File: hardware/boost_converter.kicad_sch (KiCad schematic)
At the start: 10 parts, among them U5 TPS61200DRC

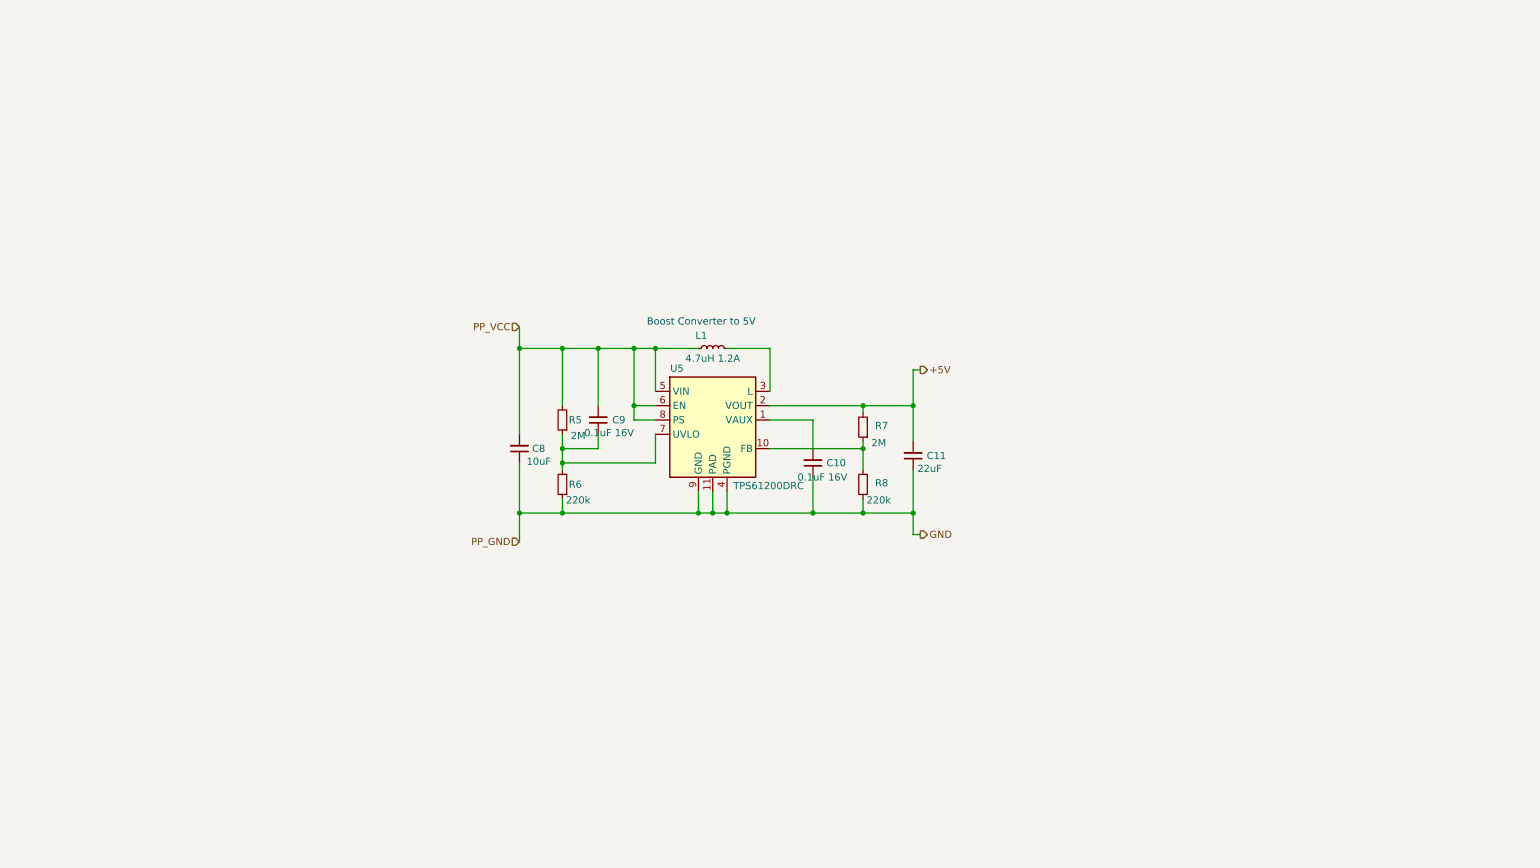
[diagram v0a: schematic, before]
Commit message: Schematic completed, commented and ready for review
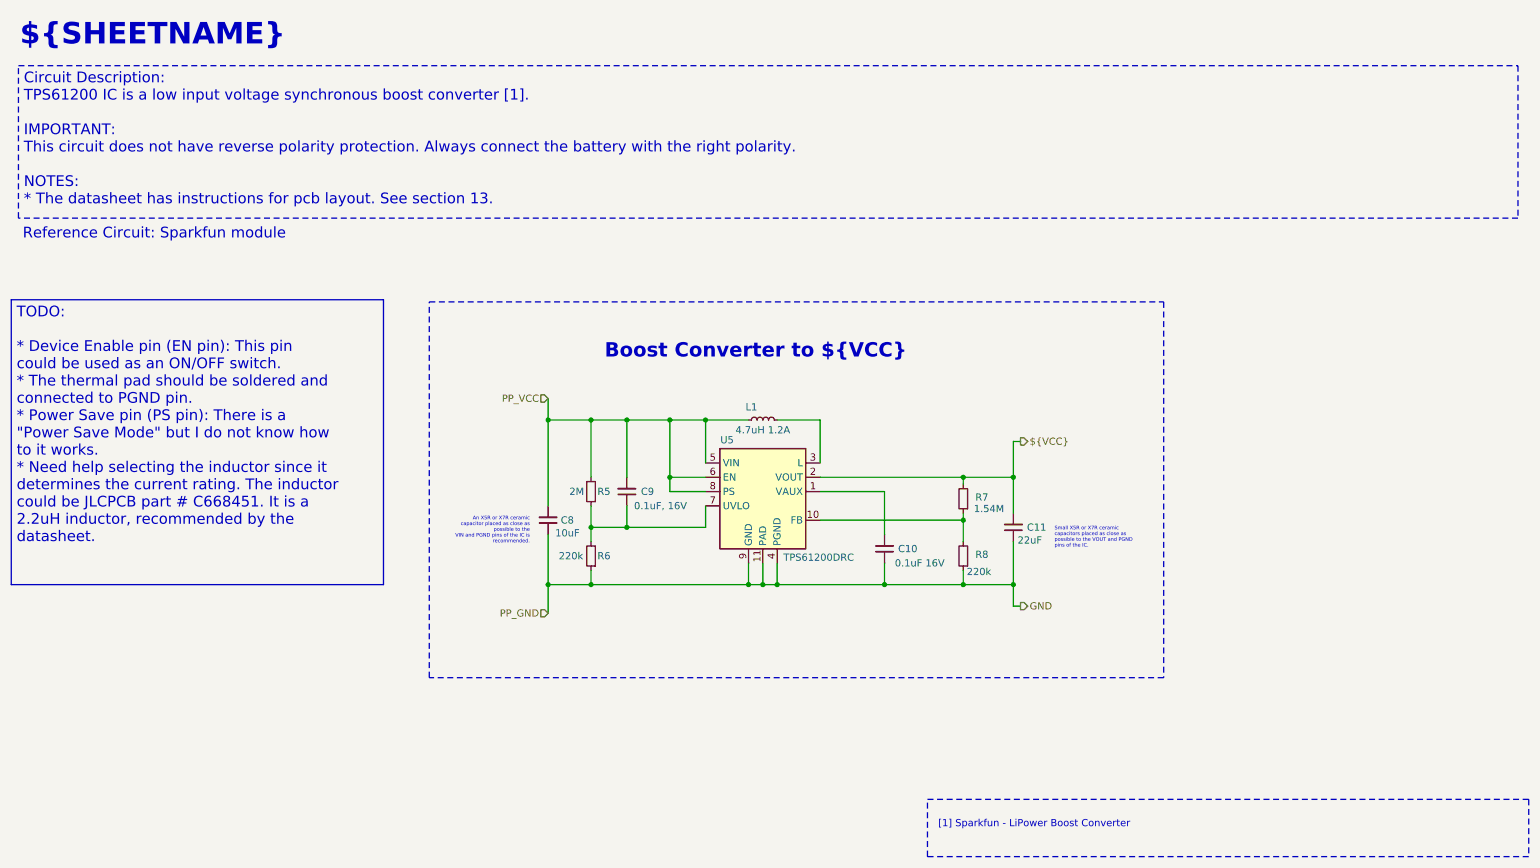
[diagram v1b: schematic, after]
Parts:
- C9: value 0.1uF 16V -> 0.1uF, 16V
- R7: value 2M -> 1.54M
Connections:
- net +5V renamed ${VCC}
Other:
- note added: "${SHEETNAME}"
- note added: "Boost Converter to ${VCC}"
- note added: "Reference Circuit: Sparkfun module"
- note added: "[1] Sparkfun - LiPower Boost Converter"
- note removed: "Boost Converter to 5V"
- title: Kitchen_Timer - 5V Boost Converter -> Kitchen_Timer - ${SHEETNAME}
- moved on the sheet: C10, C11, C8, C9, L1, R5, R6, R7, R8, U5

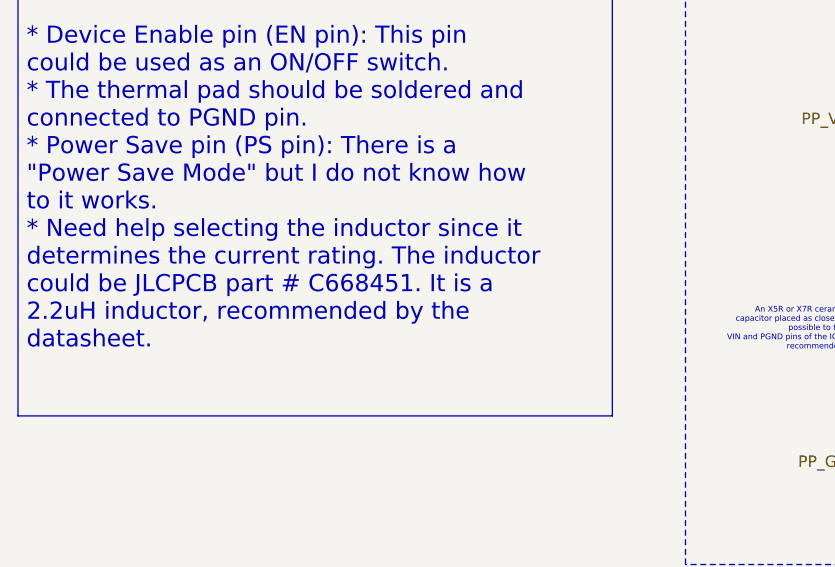
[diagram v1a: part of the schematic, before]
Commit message: Added comments to the TODO boxes after the meeting with Erasmus
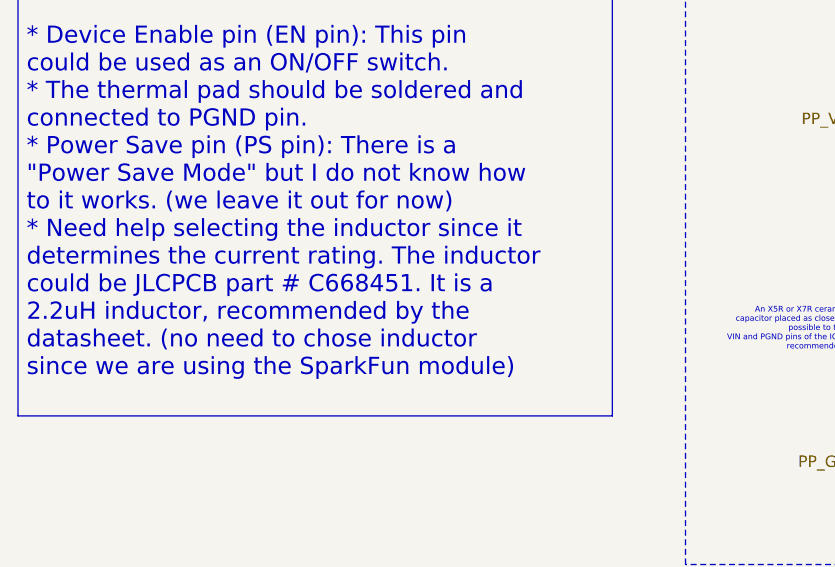
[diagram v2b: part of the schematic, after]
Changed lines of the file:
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@@
 		)
 	)
-	(text_box "TODO:\n\n* Device Enable pin (EN pin): This pin could be used as an ON/OFF switch.\n* The thermal pad should be soldered and connected to PGND pin.\n* Power Save pin (PS pin): There is a \"Power Save Mode\" but I do not know how to it works.\n* Need help selecting the inductor since it determines the current rating. The inductor could be JLCPCB part # C668451. It is a 2.2uH inductor, recommended by the datasheet.\n\n"
+	(text_box "TODO:\n\n* Device Enable pin (EN pin): This pin could be used as an ON/OFF switch.\n* The thermal pad should be soldered and connected to PGND pin.\n* Power Save pin (PS pin): There is a \"Power Save Mode\" but I do not know how to it works. (we leave it out for now)\n* Need help selecting the inductor since it determines the current rating. The inductor could be JLCPCB part # C668451. It is a 2.2uH inductor, recommended by the datasheet. (no need to chose inductor since we are using the SparkFun module)\n\n\n"
 		(exclude_from_sim no)
 		(at 15.24 66.294 0)

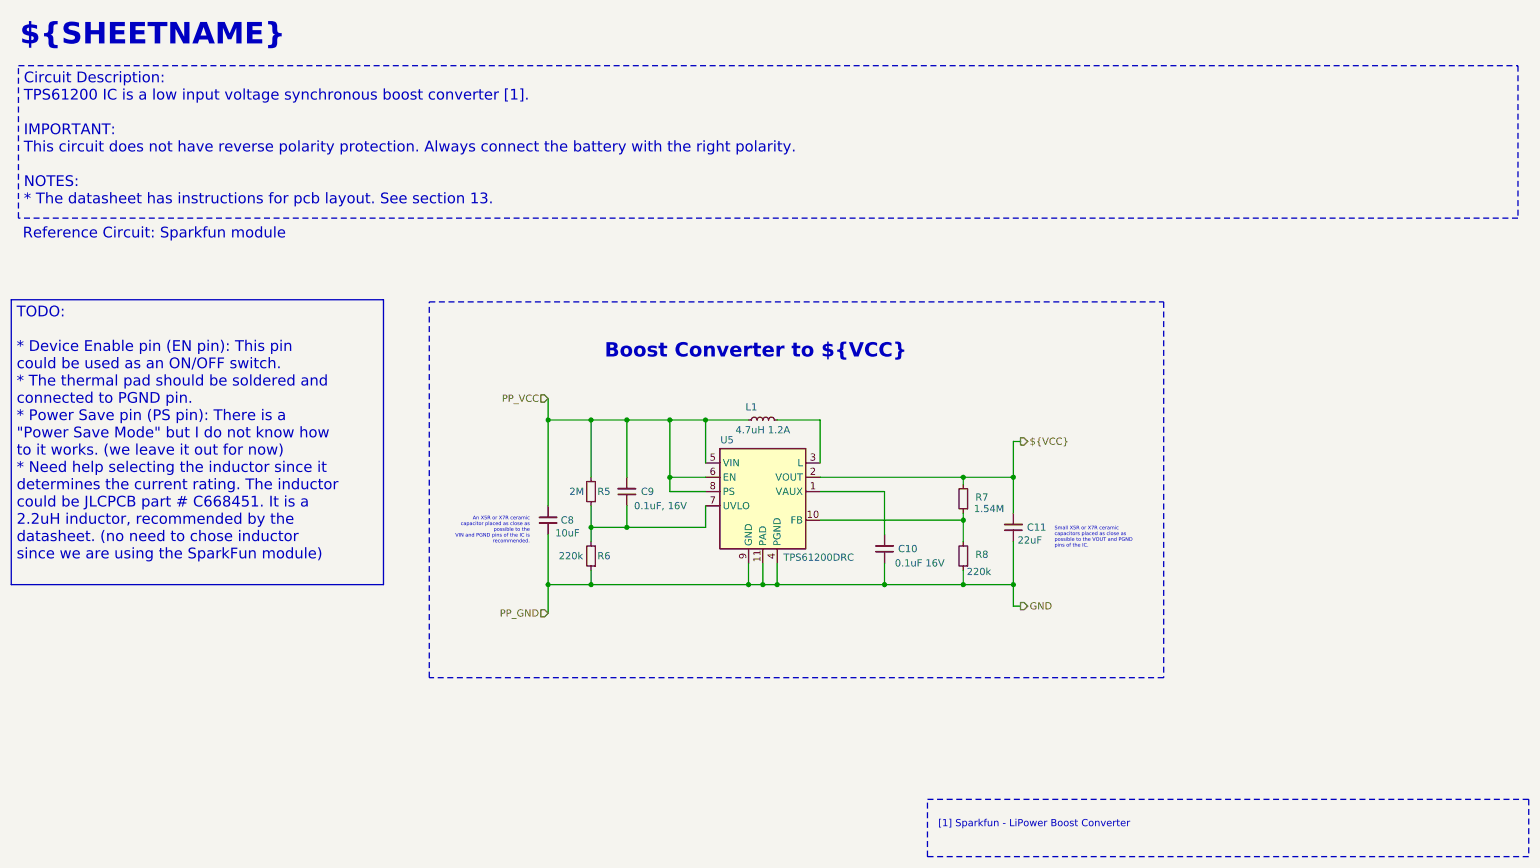
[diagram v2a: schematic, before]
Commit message: Added the Power Switch and Test Points
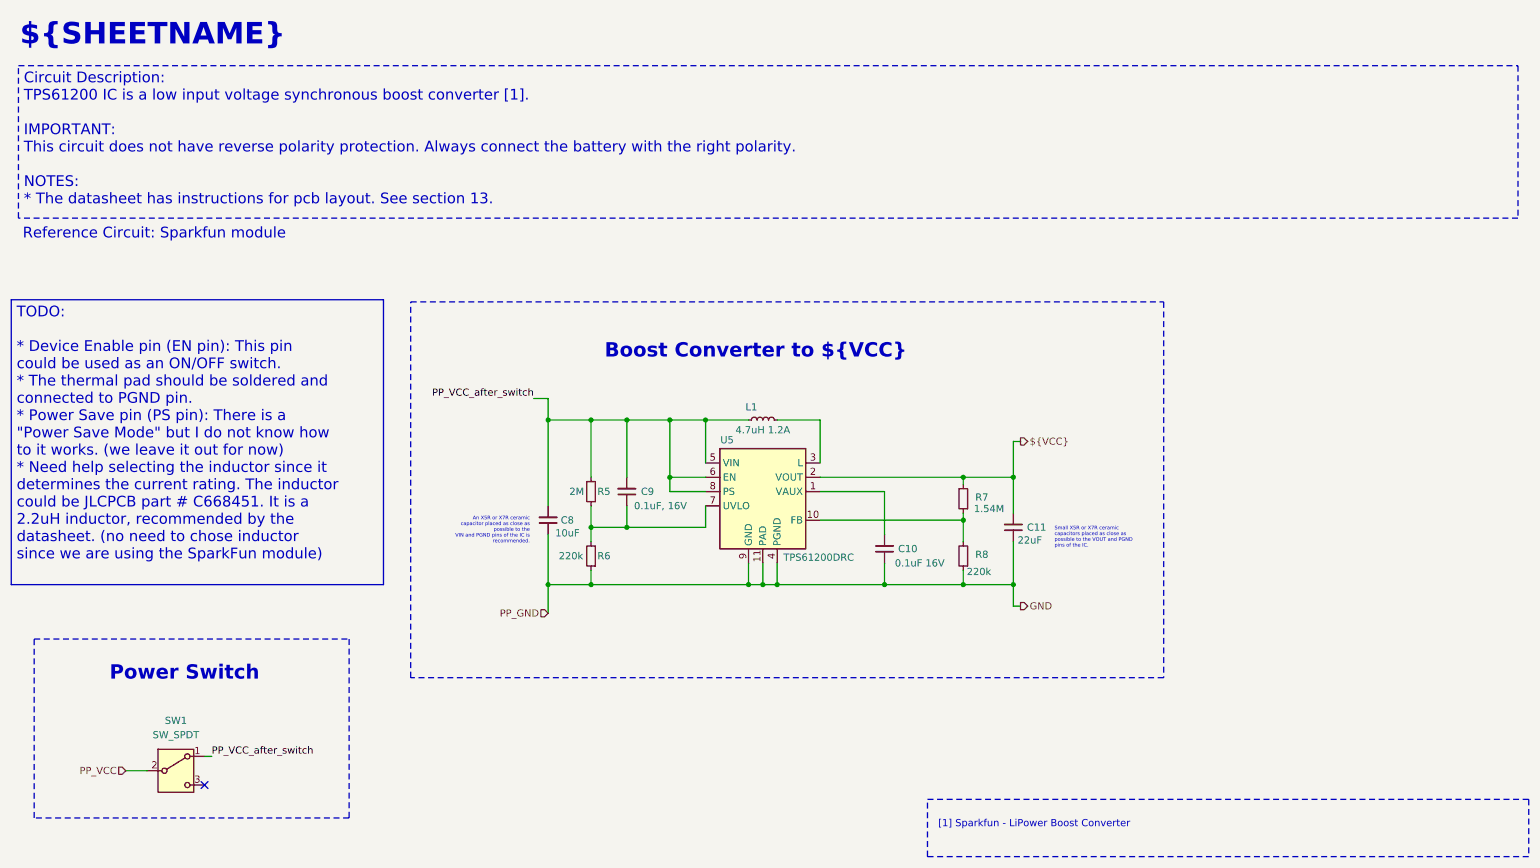
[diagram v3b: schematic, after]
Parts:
- added SW1: SW_SPDT, symbol Switch:SW_SPDT
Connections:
- net PP_VCC: now also SW1.2 (B); no longer C8.2, C9.2, L1.1, R5.2, U5.5 (VIN), U5.6 (EN), U5.8 (PS)
- new net PP_VCC_after_switch: C8.2, C9.2, L1.1, R5.2, SW1.1 (A), U5.5 (VIN), U5.6 (EN), U5.8 (PS)
- no-connect marks 0 -> 1
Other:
- note added: "Power Switch"
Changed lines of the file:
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@@
 	)
 	(rectangle
-		(start 89.408 66.675)
+		(start 19.304 126.492)
+		(end 75.184 158.242)
+		(stroke
+			(width 0)
+			(type dash)
+		)
+		(fill
+			(type none)
+		)
+	)
+	(rectangle
+		(start 86.106 66.675)
 		(end 219.71 133.35)
 		(stroke
@@
 		)
 	)
-	(text "[1] Sparkfun - LiPower Boost Converter"
-		(exclude_from_sim no)
-		(at 179.705 158.623 0)
-		(effects
-			(font
-				(size 1.27 1.27)
-				(thickness 0.1588)
-			)
-			(justify left top)
-			(href "https://www.sparkfun.com/lipower-boost-converter.html")
-		)
-	)
-	(text "Reference Circuit: Sparkfun module"
-		(exclude_from_sim no)
-		(at 17.272 54.61 0)
-		(effects
-			(font
-				(size 1.905 1.905)
-				(thickness 0.2381)
-			)
-			(justify left)
-			(href "https://cdn.sparkfun.com/datasheets/Prototyping/Li_Power_Boost_Converter.pdf")
-		)
-	)
-	(text "Boost Converter to ${VCC}"
-		(exclude_from_sim no)
-		(at 147.32 75.438 0)
+	(text "Power Switch"
+		(exclude_from_sim no)
+		(at 45.974 132.588 0)
 		(effects
 			(font
@@
 		)
 	)
+	(text "[1] Sparkfun - LiPower Boost Converter"
+		(exclude_from_sim no)
+		(at 179.705 158.623 0)
+		(effects
+			(font
+				(size 1.27 1.27)
+				(thickness 0.1588)
+			)
+			(justify left top)
+			(href "https://www.sparkfun.com/lipower-boost-converter.html")
+		)
+	)
+	(text "Reference Circuit: Sparkfun module"
+		(exclude_from_sim no)
+		(at 17.272 54.61 0)
+		(effects
+			(font
+				(size 1.905 1.905)
+				(thickness 0.2381)
+			)
+			(justify left)
+			(href "https://cdn.sparkfun.com/datasheets/Prototyping/Li_Power_Boost_Converter.pdf")
+		)
+	)
+	(text "Boost Converter to ${VCC}"
+		(exclude_from_sim no)
+		(at 147.32 75.438 0)
+		(effects
+			(font
+				(size 2.54 2.54)
+				(thickness 0.508)
+				(bold yes)
+			)
+		)
+	)
 	(text_box "An X5R or X7R ceramic capacitor placed as close as possible to the\nVIN and PGND pins of the IC is recommended."
 		(exclude_from_sim no)
@@
 		(color 0 0 0 0)
 	)
+	(no_connect
+		(at 49.53 152.4)
+	)
 	(wire
 		(pts
@@
 	(wire
 		(pts
+			(xy 35.56 149.86) (xy 39.37 149.86)
+		)
+		(stroke
+			(width 0)
+			(type default)
+		)
+	)
+	(wire
+		(pts
 			(xy 193.04 91.44) (xy 194.31 91.44)
 		)
@@
 	(wire
 		(pts
+			(xy 49.53 147.32) (xy 50.8 147.32)
+		)
+		(stroke
+			(width 0)
+			(type default)
+		)
+	)
+	(wire
+		(pts
 			(xy 118.11 102.87) (xy 118.11 106.68)
 		)
@@
 	(wire
 		(pts
+			(xy 107.95 83.82) (xy 110.49 83.82)
+		)
+		(stroke
+			(width 0)
+			(type default)
+		)
+	)
+	(wire
+		(pts
 			(xy 124.46 102.87) (xy 124.46 106.68)
 		)
@@
 			(width 0)
 			(type default)
+		)
+	)
+	(label "PP_VCC_after_switch"
+		(at 50.8 147.32 0)
+		(effects
+			(font
+				(size 1.27 1.27)
+			)
+			(justify left bottom)
+		)
+	)
+	(label "PP_VCC_after_switch"
+		(at 107.95 83.82 180)
+		(effects
+			(font
+				(size 1.27 1.27)
+			)
+			(justify right bottom)
 		)
 	)
@@
 		)
 	)
-	(hierarchical_label "PP_VCC"
-		(shape input)
-		(at 110.49 83.82 180)
-		(effects
-			(font
-				(size 1.27 1.27)
-			)
-			(justify right)
-		)
-	)
 	(hierarchical_label "PP_GND"
 		(shape input)
@@
 			)
 			(justify left)
+		)
+	)
+	(hierarchical_label "PP_VCC"
+		(shape input)
+		(at 35.56 149.86 180)
+		(effects
+			(font
+				(size 1.27 1.27)
+			)
+			(justify right)
 		)
 	)
@@
 					(unit 1)
 				)
+			)
+		)
+	)
+	(symbol
+		(lib_id "Switch:SW_SPDT")
+		(at 44.45 149.86 0)
+		(unit 1)
+		(exclude_from_sim no)
+		(in_bom yes)
+		(on_board yes)
+		(dnp no)
+		(fields_autoplaced yes)
+		(property "Reference" "SW1"
+			(at 44.45 140.97 0)
+			(effects
+				(font
+					(size 1.27 1.27)
+				)
+			)
+		)
+		(property "Value" "SW_SPDT"
+			(at 44.45 143.51 0)
+			(effects
+				(font
+					(size 1.27 1.27)
+				)
+			)
+		)
+		(property "Footprint" ""
+			(at 44.45 149.86 0)
+			(effects
+				(font
+					(size 1.27 1.27)
+				)
+				(hide yes)
+			)
+		)
+		(property "Datasheet" "~"
+			(at 44.45 157.48 0)
+			(effects
+				(font
+					(size 1.27 1.27)
+				)
+				(hide yes)
+			)
+		)
+		(property "Description" "Switch, single pole double throw"
+			(at 44.45 149.86 0)
+			(effects
+				(font
+					(size 1.27 1.27)
+				)
+				(hide yes)
+			)
+		)
+		(property "Supplier Link" "https://jlcpcb.com/partdetail/ShouHan-MSK12C02HB/C431541"
+			(at 44.45 149.86 0)
+			(effects
+				(font
+					(size 1.27 1.27)
+				)
+				(hide yes)
+			)
+		)
+		(property "Price/unit" ""
+			(at 44.45 149.86 0)
+			(effects
+				(font
+					(size 1.27 1.27)
+				)
+				(hide yes)
+			)
+		)
+		(property "Part Num" ""
+			(at 44.45 149.86 0)
+			(effects
+				(font
+					(size 1.27 1.27)
+				)
+				(hide yes)
+			)
+		)
+		(property "Package" ""
+			(at 44.45 149.86 0)
+			(effects
+				(font
+					(size 1.27 1.27)
+				)
+				(hide yes)
+			)
+		)
+		(pin "3"
+		)
+		(pin "1"
+		)
+		(pin "2"
+		)
+		(instances
+			(project ""
+				(path "/8963deea-96bc-4401-b671-98fbe9ed9c6a/8d96c6df-7eb2-480a-982a-3dd8886e54b6"
+					(reference "SW1")
+					(unit 1)
+				)
